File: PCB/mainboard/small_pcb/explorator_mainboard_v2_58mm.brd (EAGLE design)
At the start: 58 x 58 mm, 59 parts, among them CN11 0.1uf, CN12 0.1uf, CN13 0.1uf, CN14 0.1uf, CN15 0.1uf, CN16 0.1uf, CN17 0.1uf, CN18 0.1uf, CN19 0.1uf, CN20 0.1uf, M1 5566-2, P1 B10B-PH-K, P2 B4B-PH-K, Q1 PNO8L07, Q2 PNO8L07, U2 SHTC3

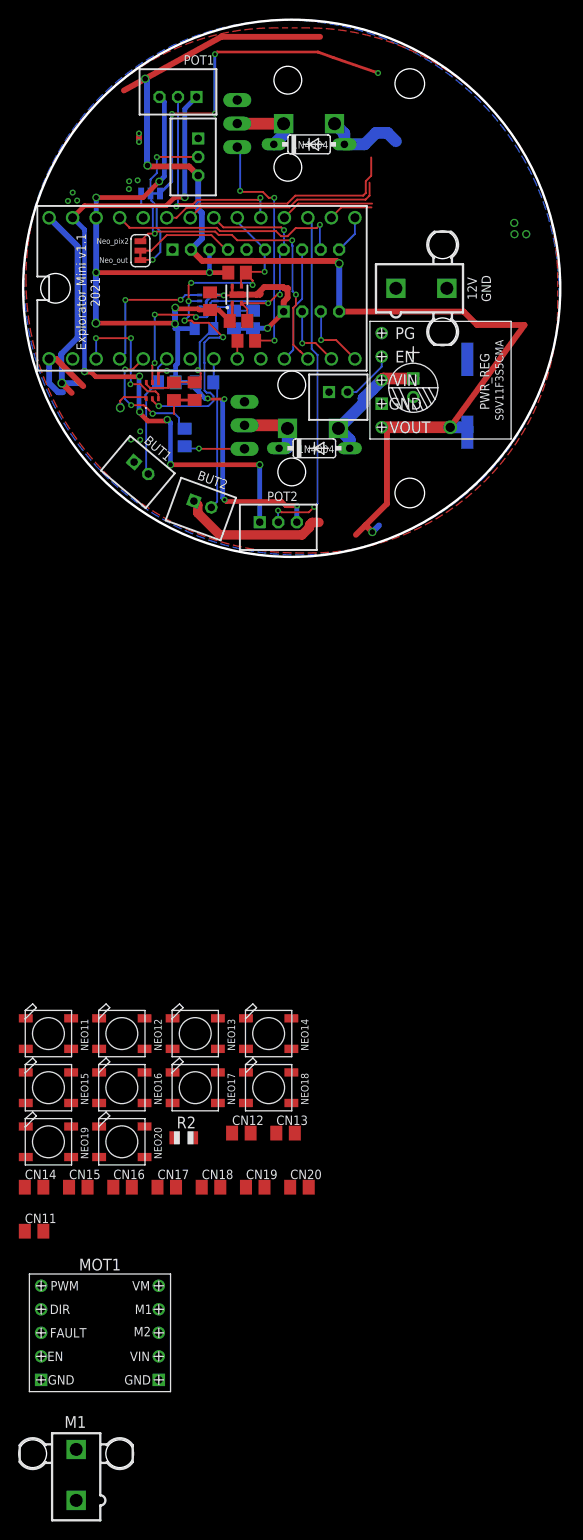
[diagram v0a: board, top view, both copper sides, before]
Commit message: updated the mainboard's with the new information found in other folders including net_lists, parts_lists, pin_lists, and such
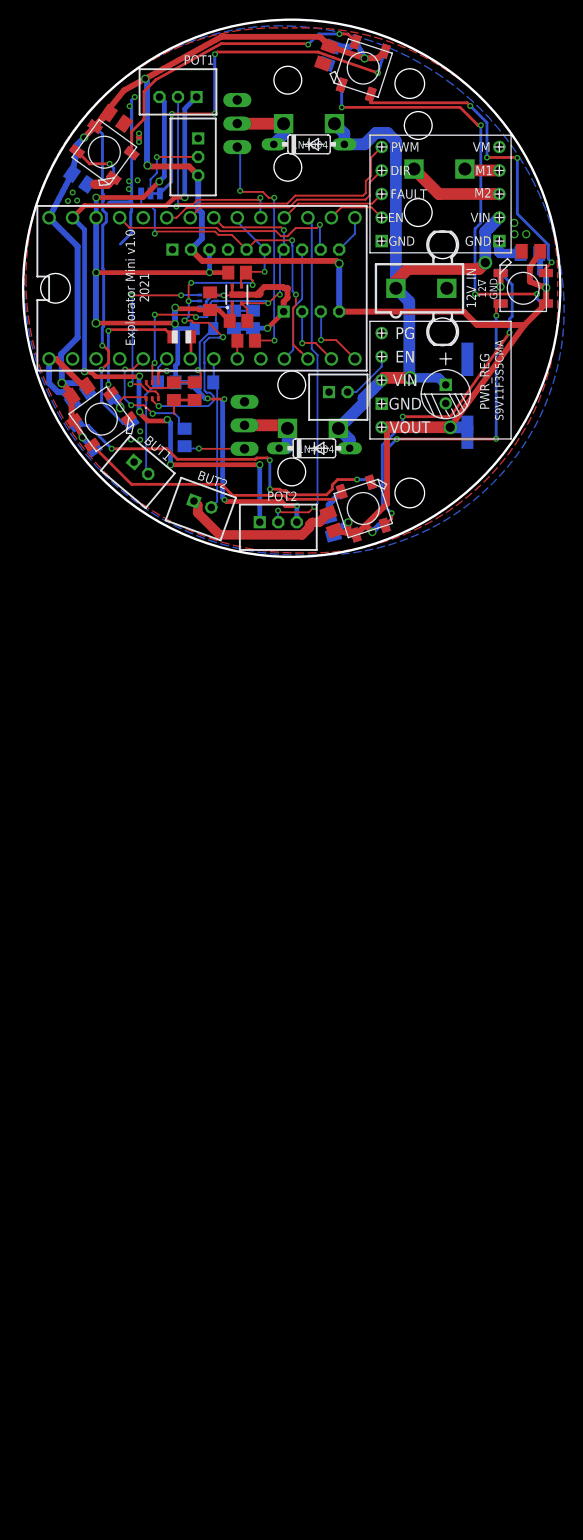
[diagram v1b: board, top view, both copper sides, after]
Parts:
- removed CN11, CN12, CN13, CN14, CN15, CN16, CN17, CN18, CN19, CN20: 0.1uf, resistor:C0805K
- removed JP2: JUMPER-SMT_3_1-NC_TRACE_SILK, SparkFun-Jumpers:SMT-JUMPER_3_1-NC_TRACE_SILK
- removed NEO11, NEO12, NEO13, NEO14, NEO15, NEO16, NEO17, NEO18, NEO19, NEO20: WS2812B5050, nathans-custom-parts:WS2812B
- removed R2: 300 R, audio amplifier example:R0805
- added CN1, CN10, CN2, CN3, CN4, CN5, CN6, CN7, CN8, CN9: 0.1uf, resistor:C0805K
- added NEO1, NEO10, NEO2, NEO3, NEO4, NEO5, NEO6, NEO7, NEO8, NEO9: WS2812B5050, nathans-custom-parts:WS2812B
- added R5: 300 R, audio amplifier example:R0805
- moved M1 146.3 mm to (16.0, 12.9), flipped to the bottom, turned to 270 degrees
- moved MOT1 128.3 mm to (16.1, 10.2)
- moved C2 3.57 mm to (16.6, -11.4)
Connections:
- removed net N$17: NEO14.2-DOUT, NEO15.4-DIN
- removed net N$18: NEO12.4-DIN, NEO15.2-DOUT
- removed net N$19: NEO11.4-DIN, NEO12.2-DOUT
- removed net N$20: NEO11.2-DOUT, NEO13.4-DIN
- removed net N$21: NEO13.2-DOUT, NEO18.4-DIN
- removed net N$22: NEO14.4-DIN, R2.1
- removed net N$23: NEO18.2-DOUT, NEO19.4-DIN
- removed net N$26: NEO19.2-DOUT, NEO20.4-DIN
- removed net N$27: NEO16.4-DIN, NEO20.2-DOUT
- removed net N$28: NEO16.2-DOUT, NEO17.4-DIN
- removed net NOUT_01: JP2.2, P1.4
- removed net VEML_INT1: U$1.2, VMEL1.3
- removed net VEML_INT2: U$1.1, VMEL2.3
- new net INT: VMEL1.3, VMEL2.3
- new net N$1: NEO4.2-DOUT, NEO5.4-DIN
- new net N$11: NEO8.2-DOUT, NEO9.4-DIN
- new net N$12: NEO10.4-DIN, NEO9.2-DOUT
- new net N$15: NEO10.2-DOUT, NEO6.4-DIN
- new net N$16: NEO6.2-DOUT, NEO7.4-DIN
- new net N$2: NEO1.4-DIN, NEO5.2-DOUT
- new net N$4: NEO1.2-DOUT, NEO2.4-DIN
- new net N$5: NEO2.2-DOUT, NEO3.4-DIN
- new net N$6: NEO3.2-DOUT, NEO8.4-DIN
- new net N$8: NEO4.4-DIN, R5.1
- new net NOUT: P1.4
- net 5V: now also CN1.1, CN10.1, CN2.1, CN3.1, CN4.1, CN5.1, CN6.1, CN7.1, CN8.1, CN9.1, NEO1.1-VDD, NEO10.1-VDD, NEO2.1-VDD, NEO3.1-VDD, NEO4.1-VDD, NEO5.1-VDD, NEO6.1-VDD, NEO7.1-VDD, NEO8.1-VDD, NEO9.1-VDD; no longer CN11.1, CN12.1, CN13.1, CN14.1, CN15.1, CN16.1, CN17.1, CN18.1, CN19.1, CN20.1, NEO11.1-VDD, NEO12.1-VDD, NEO13.1-VDD, NEO14.1-VDD, NEO15.1-VDD, NEO16.1-VDD, NEO17.1-VDD, NEO18.1-VDD, NEO19.1-VDD, NEO20.1-VDD
- net GND: now also CN1.2, CN10.2, CN2.2, CN3.2, CN4.2, CN5.2, CN6.2, CN7.2, CN8.2, CN9.2, NEO1.3-GND, NEO10.3-GND, NEO2.3-GND, NEO3.3-GND, NEO4.3-GND, NEO5.3-GND, NEO6.3-GND, NEO7.3-GND, NEO8.3-GND, NEO9.3-GND; no longer CN11.2, CN12.2, CN13.2, CN14.2, CN15.2, CN16.2, CN17.2, CN18.2, CN19.2, CN20.2, NEO11.3-GND, NEO12.3-GND, NEO13.3-GND, NEO14.3-GND, NEO15.3-GND, NEO16.3-GND, NEO17.3-GND, NEO18.3-GND, NEO19.3-GND, NEO20.3-GND
- net NEO1_OUT: now also NEO7.2-DOUT; no longer NEO17.2-DOUT
- net NEO_OUT: no longer JP2.3
- net NEO_PIX1: now also R5.2; no longer R2.2
- net NEO_PIX2: now also P1.5; no longer JP2.1
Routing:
- net 5V: track 151.2 -> 211.9 mm, vias 6 -> 11
- net 12V: track 22.6 -> 69.2 mm, vias 0 -> 2
- net N$16: track 0.00 -> 45.3 mm, vias 0 -> 4
- net GND: track 58.4 -> 97.8 mm, vias 17 -> 20
- net N$15: track 0.00 -> 38.2 mm, vias 0 -> 2
- net N$12: track 0.00 -> 37.8 mm, vias 0 -> 4
- net N$2: track 0.00 -> 35.8 mm, vias 0 -> 4
- net N$4: track 0.00 -> 35.6 mm, vias 0 -> 4
- net N$11: track 0.00 -> 35.4 mm, vias 0 -> 2
- net N$5: track 0.00 -> 32.5 mm, vias 0 -> 2
- net N$1: track 0.00 -> 29.7 mm
- net INT: track 0.00 -> 21.0 mm, vias 0 -> 3
- net VEML_INT2: track 15.0 -> 0.00 mm, vias 3 -> 0
- net VEML_INT1: track 14.9 -> 0.00 mm, vias 2 -> 0
- net N$8: track 0.00 -> 14.2 mm, vias 0 -> 2
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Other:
- board text added: "Explorator Mini v1.0 2021"
- board text removed: "Explorator Mini v1.1 2021"
- board text removed: "Neo_out"
- board text removed: "Neo_pix2"
